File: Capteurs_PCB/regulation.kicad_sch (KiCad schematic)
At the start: 12 parts, among them U4 RS PRO 1W isolated DC-DC conv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, U5 RS PRO 1W isolated DC-DC conv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

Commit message: pcb update
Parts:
- removed C10, C11: 4,7pF, symbol Device:C_Small
- removed C13: 270 pF, symbol Device:C_Small
- removed L1, L3: 6,8uH, symbol Device:L_Small
- added C9: 2.2uF/25V, symbol Device:C_Small
- added U1: RS PRO 1W isolated DC-DC converters 12V, Package_TO_SOT_THT:TO-220-4_Vertical, symbol Regulator_Linear:KA378R05
- C1: renamed from C12; value 10uF -> 10uF/16V
- C2: value 4,7pF -> 1uF/50V
- C3: value 4,7pF -> 10uF/16V
- C4: value 10uF -> 1uF/50V
- C5: value 270 pF -> 1uF/50V
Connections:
- net V_5V: now also C3.2; no longer C4.2
- net Vbatterie: now also C4.2, C5.2, U4.1 (IN), U5.1 (IN), U1.1 (IN)
- removed net Earth: C2.1, C3.1, C5.2, U4.3 (GND), U5.3 (GND)
- new net: C3.1, U4.4 (0V)
- new net: C2.1, U4.3 (GND)
- new net: C4.1, U5.3 (GND)
- new net: C5.1, U1.3 (GND)
- new net: C9.1, U1.4 (0V)
- new net V_12V: C9.2, U1.2 (OUT)
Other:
- moved on the sheet: C1

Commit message: updates pcb
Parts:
- C0: renamed from C1; footprint (none) -> Capacitor_SMD:CP_Elec_4x5.4
- C2, C3, C4, C5, C9: footprint (none) -> Capacitor_SMD:CP_Elec_4x5.4
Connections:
- net Earth: now reaches C3.1, U4.4 (0V)
- net Earth: now also C0.1, C2.1, C4.1, C5.1, C9.1, U1.3 (GND), U1.4 (0V), U4.3 (GND), U5.3 (GND), U5.4 (0V)

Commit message: update pcb
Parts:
- removed C0, C3: 10uF/16V, Capacitor_SMD:CP_Elec_4x5.4, symbol Device:C_Small
- removed C2, C4, C5: 1uF/50V, Capacitor_SMD:CP_Elec_4x5.4, symbol Device:C_Small
- removed C9: 2.2uF/25V, Capacitor_SMD:CP_Elec_4x5.4, symbol Device:C_Small
- removed U1: RS PRO 1W isolated DC-DC converters 12V, Package_TO_SOT_THT:TO-220-4_Vertical, symbol Regulator_Linear:KA378R05
- removed U4: RS PRO 1W isolated DC-DC converters 5V, Package_TO_SOT_THT:TO-220-4_Vertical, symbol Regulator_Linear:KA378R05
- removed U5: RS PRO 1W isolated DC-DC converters 3V3, Package_TO_SOT_THT:TO-220-4_Vertical, symbol Regulator_Linear:KA378R05
- added C401, C405: 1u, symbol Device:C_Small
- added C402, C406: 47u, Capacitor_SMD:CP_Elec_6.3x5.4, symbol Device:C_Polarized_Small
- added C403, C404: 10u, Capacitor_SMD:CP_Elec_5x5.4, symbol Device:C_Polarized_Small
- added C407, C408: C_Small, symbol Device:C_Small
- added D401, D402, D403: LED, symbol Device:LED
- added R401, R404: 5.6k, symbol Device:R_Small
- added R402, R405: RFBT, symbol Device:R_Small
- added R403, R406: RFBB, symbol Device:R_Small
- added R407, R408, R409: R_Small, symbol Device:R_Small
- added U401, U402: ~, symbol custom:171013801
- added U403: AMS1117-3.3, Package_TO_SOT_SMD:SOT-223-3_TabPin2, symbol Regulator_Linear:AMS1117-3.3
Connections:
- new net: R401.2, U401.1 (FSW)
- new net: R402.2, R403.1, U401.2 (FB)
- new net: D402.2 (A), R408.2
- new net: C405.2, U402.3 (Vcc)
- new net: D401.2 (A), R407.2
- new net: D403.2 (A), R409.2
- new net: R404.2, U402.1 (FSW)
- new net: R405.2, R406.1, U402.2 (FB)
- new net: U402.12 (En), U402.9 (Vin_link)
- new net: U401.12 (En), U401.9 (Vin_link)
- new net: C401.2, U401.3 (Vcc)
- new net 3.3V: C408.1, R409.1, U403.2 (VO)
- new net 5.1V: C402.1, C407.1, R402.1, R408.1, U401.6 (Vout), U401.7 (Vout), U403.3 (VI)
- new net 7.4V: C406.1, R405.1, R407.1, U402.6 (Vout), U402.7 (Vout)
- new net GND: C401.1, C402.2, C403.2, C404.2, C405.1, C406.2, C407.2, C408.2, D401.1 (K), D402.1 (K), D403.1 (K), R401.1, R403.2, R404.1, R406.2, U401.10 (AGND), U401.13 (PGND), U402.10 (AGND), U402.13 (PGND), U403.1 (GND)
- new net Vin: C403.1, C404.1, U401.4 (Vin), U401.5 (Vin), U402.4 (Vin), U402.5 (Vin)
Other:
- note added: "171013801 https://www.we-online.com/components/products/datasheet/171013801.pdf https://www.we-online.com/en/components/products/MAGIC-VDRM"
- note added: "Vout = Vref * (RFBT/RFBB+1) Vref = 0.85V"

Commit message: Modif PCB
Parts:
- R402: value RFBT -> 80.4
- R403: value RFBB -> 402k
- RFBB: renamed from R406; value RFBB -> 402k
- RFBT: renamed from R405; value RFBT -> 52.2k
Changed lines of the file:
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@@
       (effects (font (size 1.27 1.27)) hide)
     )
-    (pin "2")
-    (pin "1")
+    (pin "1")
+    (pin "2")
     (instances
       (project "Capteurs_PCB"
@@
   (symbol (lib_id "Device:R_Small") (at 104.14 116.84 0) (unit 1)
     (in_bom yes) (on_board yes) (dnp no) (fields_autoplaced)
-    (property "Reference" "R403" (at 106.68 115.57 0)
-      (effects (font (size 1.27 1.27)) (justify left))
-    )
-    (property "Value" "RFBB" (at 106.68 118.11 0)
+    (property "Reference" "R403" (at 106.68 116.205 0)
+      (effects (font (size 1.27 1.27)) (justify left))
+    )
+    (property "Value" "402k" (at 106.68 118.745 0)
       (effects (font (size 1.27 1.27)) (justify left))
     )
@@
       (effects (font (size 1.27 1.27)) hide)
     )
-    (pin "2")
-    (pin "1")
+    (pin "1")
+    (pin "2")
     (instances
       (project "Capteurs_PCB"
@@
       (effects (font (size 1.27 1.27)) hide)
     )
-    (pin "2")
-    (pin "1")
+    (pin "1")
+    (pin "2")
     (instances
       (project "Capteurs_PCB"
@@
       (effects (font (size 1.27 1.27)) hide)
     )
-    (pin "2")
-    (pin "1")
+    (pin "1")
+    (pin "2")
     (instances
       (project "Capteurs_PCB"
@@
       (effects (font (size 1.27 1.27)) hide)
     )
-    (pin "2")
-    (pin "1")
+    (pin "1")
+    (pin "2")
     (instances
       (project "Capteurs_PCB"
@@
       (effects (font (size 1.27 1.27)) hide)
     )
-    (pin "2")
-    (pin "1")
+    (pin "1")
+    (pin "2")
     (instances
       (project "Capteurs_PCB"
@@
   (symbol (lib_id "Device:R_Small") (at 104.14 71.12 0) (unit 1)
     (in_bom yes) (on_board yes) (dnp no) (fields_autoplaced)
-    (property "Reference" "R406" (at 106.68 69.85 0)
-      (effects (font (size 1.27 1.27)) (justify left))
-    )
-    (property "Value" "RFBB" (at 106.68 72.39 0)
+    (property "Reference" "RFBB" (at 106.68 70.485 0)
+      (effects (font (size 1.27 1.27)) (justify left))
+    )
+    (property "Value" "402k" (at 106.68 73.025 0)
       (effects (font (size 1.27 1.27)) (justify left))
     )
@@
       (project "Capteurs_PCB"
         (path "/1101af8f-9425-4102-9245-339dc54562bf/b84a61ef-89d4-47b7-a16e-5e36daa53b0c"
-          (reference "R406") (unit 1)
+          (reference "RFBB") (unit 1)
         )
       )
@@
       (effects (font (size 1.27 1.27)) hide)
     )
-    (pin "2")
-    (pin "1")
+    (pin "1")
+    (pin "2")
     (instances
       (project "Capteurs_PCB"
@@
   (symbol (lib_id "Device:R_Small") (at 104.14 109.22 0) (unit 1)
     (in_bom yes) (on_board yes) (dnp no) (fields_autoplaced)
-    (property "Reference" "R402" (at 106.68 107.95 0)
-      (effects (font (size 1.27 1.27)) (justify left))
-    )
-    (property "Value" "RFBT" (at 106.68 110.49 0)
+    (property "Reference" "R402" (at 106.68 108.585 0)
+      (effects (font (size 1.27 1.27)) (justify left))
+    )
+    (property "Value" "80.4" (at 106.68 111.125 0)
       (effects (font (size 1.27 1.27)) (justify left))
     )
@@
       (effects (font (size 1.27 1.27)) hide)
     )
-    (pin "2")
-    (pin "1")
+    (pin "1")
+    (pin "2")
     (instances
       (project "Capteurs_PCB"
@@
       (effects (font (size 1.27 1.27)) hide)
     )
+    (pin "1")
+    (pin "10")
     (pin "11")
+    (pin "12")
+    (pin "13")
+    (pin "2")
+    (pin "3")
+    (pin "4")
+    (pin "5")
     (pin "6")
-    (pin "12")
-    (pin "5")
     (pin "7")
     (pin "9")
+    (instances
+      (project "Capteurs_PCB"
+        (path "/1101af8f-9425-4102-9245-339dc54562bf/b84a61ef-89d4-47b7-a16e-5e36daa53b0c"
+          (reference "U402") (unit 1)
+        )
+      )
+    )
+  )
+  (symbol (lib_id "power:GND") (at 213.36 91.44 0) (unit 1)
+    (in_bom yes) (on_board yes) (dnp no) (fields_autoplaced)
+    (property "Reference" "#PWR0414" (at 213.36 97.79 0)
+      (effects (font (size 1.27 1.27)) hide)
+    )
+    (property "Value" "GND" (at 213.36 96.52 0)
+      (effects (font (size 1.27 1.27)))
+    )
+    (property "Footprint" "" (at 213.36 91.44 0)
+      (effects (font (size 1.27 1.27)) hide)
+    )
+    (property "Datasheet" "" (at 213.36 91.44 0)
+      (effects (font (size 1.27 1.27)) hide)
+    )
+    (pin "1")
+    (instances
+      (project "Capteurs_PCB"
+        (path "/1101af8f-9425-4102-9245-339dc54562bf/b84a61ef-89d4-47b7-a16e-5e36daa53b0c"
+          (reference "#PWR0414") (unit 1)
+        )
+      )
+    )
+  )
+  (symbol (lib_id "custom:171013801") (at 86.36 109.22 0) (unit 1)
+    (in_bom yes) (on_board yes) (dnp no) (fields_autoplaced)
+    (property "Reference" "U401" (at 86.36 92.71 0)
+      (effects (font (size 1.27 1.27)))
+    )
+    (property "Value" "~" (at 86.36 99.06 0)
+      (effects (font (size 1.27 1.27)))
+    )
+    (property "Footprint" "" (at 86.36 99.06 0)
+      (effects (font (size 1.27 1.27)) hide)
+    )
+    (property "Datasheet" "https://www.we-online.com/components/products/datasheet/171013801.pdf" (at 86.36 99.06 0)
+      (effects (font (size 1.27 1.27)) hide)
+    )
+    (property "MPN" "171013801" (at 86.36 109.22 0)
+      (effects (font (size 1.27 1.27)) hide)
+    )
+    (pin "1")
     (pin "10")
-    (pin "1")
+    (pin "11")
+    (pin "12")
+    (pin "13")
+    (pin "2")
     (pin "3")
     (pin "4")
-    (pin "2")
-    (pin "13")
-    (instances
-      (project "Capteurs_PCB"
-        (path "/1101af8f-9425-4102-9245-339dc54562bf/b84a61ef-89d4-47b7-a16e-5e36daa53b0c"
-          (reference "U402") (unit 1)
-        )
-      )
-    )
-  )
-  (symbol (lib_id "power:GND") (at 213.36 91.44 0) (unit 1)
-    (in_bom yes) (on_board yes) (dnp no) (fields_autoplaced)
-    (property "Reference" "#PWR0414" (at 213.36 97.79 0)
-      (effects (font (size 1.27 1.27)) hide)
-    )
-    (property "Value" "GND" (at 213.36 96.52 0)
-      (effects (font (size 1.27 1.27)))
-    )
-    (property "Footprint" "" (at 213.36 91.44 0)
-      (effects (font (size 1.27 1.27)) hide)
-    )
-    (property "Datasheet" "" (at 213.36 91.44 0)
-      (effects (font (size 1.27 1.27)) hide)
-    )
-    (pin "1")
-    (instances
-      (project "Capteurs_PCB"
-        (path "/1101af8f-9425-4102-9245-339dc54562bf/b84a61ef-89d4-47b7-a16e-5e36daa53b0c"
-          (reference "#PWR0414") (unit 1)
-        )
-      )
-    )
-  )
-  (symbol (lib_id "custom:171013801") (at 86.36 109.22 0) (unit 1)
-    (in_bom yes) (on_board yes) (dnp no) (fields_autoplaced)
-    (property "Reference" "U401" (at 86.36 92.71 0)
-      (effects (font (size 1.27 1.27)))
-    )
-    (property "Value" "~" (at 86.36 99.06 0)
-      (effects (font (size 1.27 1.27)))
-    )
-    (property "Footprint" "" (at 86.36 99.06 0)
-      (effects (font (size 1.27 1.27)) hide)
-    )
-    (property "Datasheet" "https://www.we-online.com/components/products/datasheet/171013801.pdf" (at 86.36 99.06 0)
-      (effects (font (size 1.27 1.27)) hide)
-    )
-    (property "MPN" "171013801" (at 86.36 109.22 0)
-      (effects (font (size 1.27 1.27)) hide)
-    )
-    (pin "11")
+    (pin "5")
     (pin "6")
-    (pin "12")
-    (pin "5")
     (pin "7")
     (pin "9")
-    (pin "10")
-    (pin "1")
-    (pin "3")
-    (pin "4")
-    (pin "2")
-    (pin "13")
     (instances
       (project "Capteurs_PCB"
@@
       (effects (font (size 1.27 1.27)) hide)
     )
-    (pin "2")
-    (pin "1")
+    (pin "1")
+    (pin "2")
     (instances
       (project "Capteurs_PCB"
@@
       (effects (font (size 1.27 1.27)) hide)
     )
-    (pin "2")
-    (pin "1")
+    (pin "1")
+    (pin "2")
     (instances
       (project "Capteurs_PCB"
@@
       (effects (font (size 1.27 1.27)) hide)
     )
-    (pin "2")
-    (pin "1")
+    (pin "1")
+    (pin "2")
     (instances
       (project "Capteurs_PCB"
@@
       (effects (font (size 1.27 1.27)) hide)
     )
-    (pin "2")
-    (pin "1")
+    (pin "1")
+    (pin "2")
     (instances
       (project "Capteurs_PCB"
@@
   (symbol (lib_id "Device:R_Small") (at 104.14 63.5 0) (unit 1)
     (in_bom yes) (on_board yes) (dnp no) (fields_autoplaced)
-    (property "Reference" "R405" (at 106.68 62.23 0)
-      (effects (font (size 1.27 1.27)) (justify left))
-    )
-    (property "Value" "RFBT" (at 106.68 64.77 0)
+    (property "Reference" "RFBT" (at 106.68 62.865 0)
+      (effects (font (size 1.27 1.27)) (justify left))
+    )
+    (property "Value" "52.2k" (at 106.68 65.405 0)
       (effects (font (size 1.27 1.27)) (justify left))
     )
@@
       (project "Capteurs_PCB"
         (path "/1101af8f-9425-4102-9245-339dc54562bf/b84a61ef-89d4-47b7-a16e-5e36daa53b0c"
-          (reference "R405") (unit 1)
-        )
-      )
+          (reference "RFBT") (unit 1)
+        )
+      )

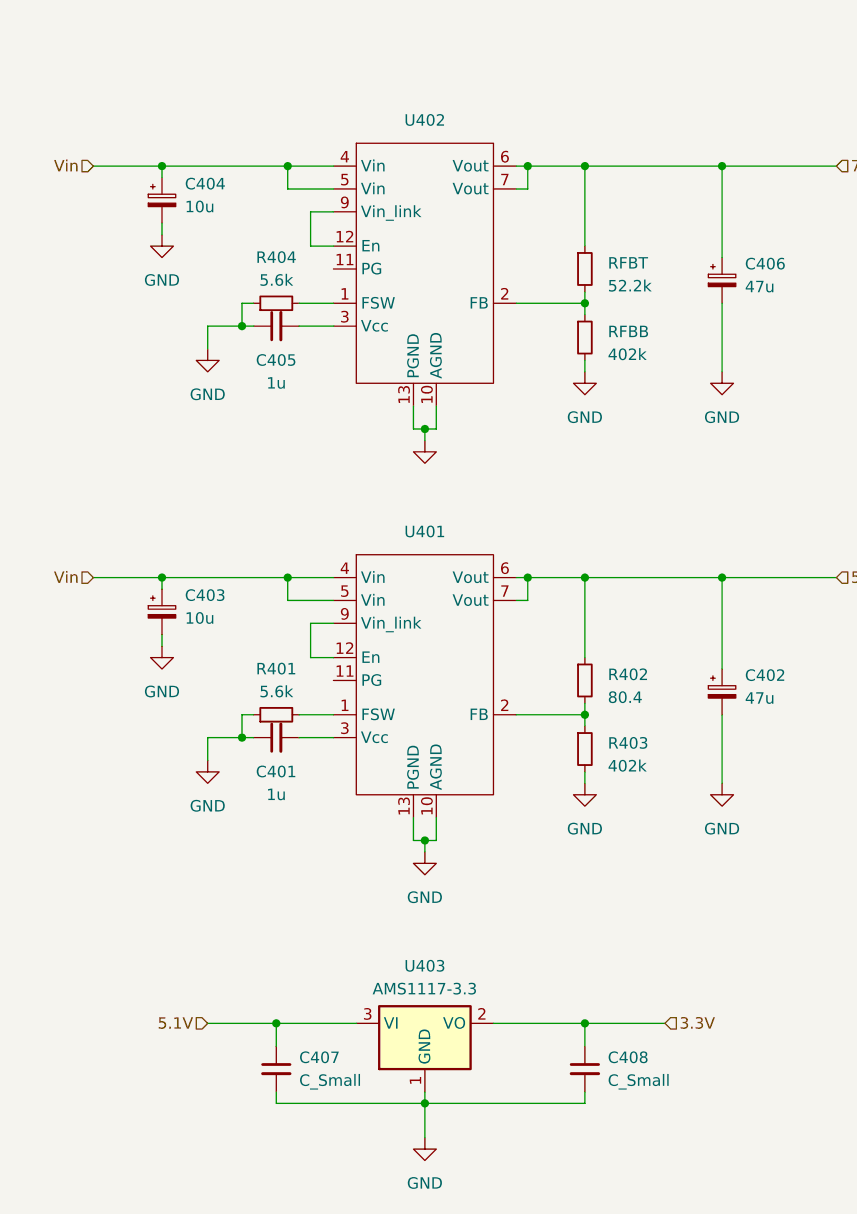
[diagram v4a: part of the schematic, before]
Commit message: kicad changes and starting footprints
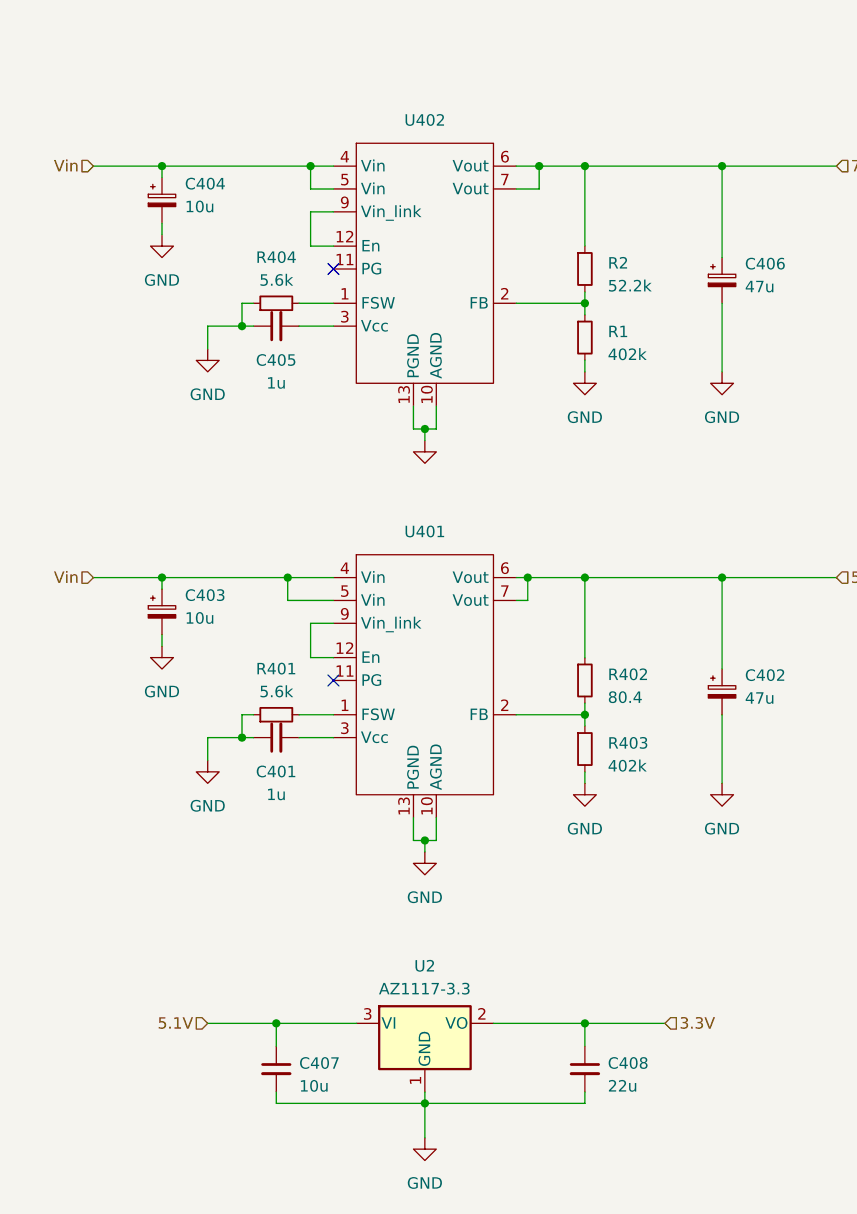
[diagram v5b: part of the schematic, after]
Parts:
- removed RFBB: 402k, symbol Device:R_Small
- removed RFBT: 52.2k, symbol Device:R_Small
- removed U403: AMS1117-3.3, Package_TO_SOT_SMD:SOT-223-3_TabPin2, symbol Regulator_Linear:AMS1117-3.3
- added R1: 402k, symbol Device:R_Small
- added R2: 52.2k, symbol Device:R_Small
- added U2: AZ1117-3.3, symbol Regulator_Linear:AZ1117-3.3
- C401, C405: footprint (none) -> Capacitor_SMD:C_1206_3216Metric
- C407: value C_Small -> 10u; footprint (none) -> Capacitor_SMD:C_1206_3216Metric
- C408: value C_Small -> 22u; footprint (none) -> Capacitor_SMD:C_1206_3216Metric
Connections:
- net 3.3V: now also U2.2 (VO)
- net 5.1V: now also U2.3 (VI)
- net 7.4V: now also R2.1
- net GND: now also R1.2, U2.1 (GND)
- net at U402.2 (FB): now also R1.1, R2.2
- no-connect marks 0 -> 2
